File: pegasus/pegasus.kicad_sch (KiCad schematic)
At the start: 14 parts, among them IC4 L70B-M39, IC5 L7805ACV, J1 Conn_01x02_Female, J2 Conn_01x02_Female, U1 Teensy4.1

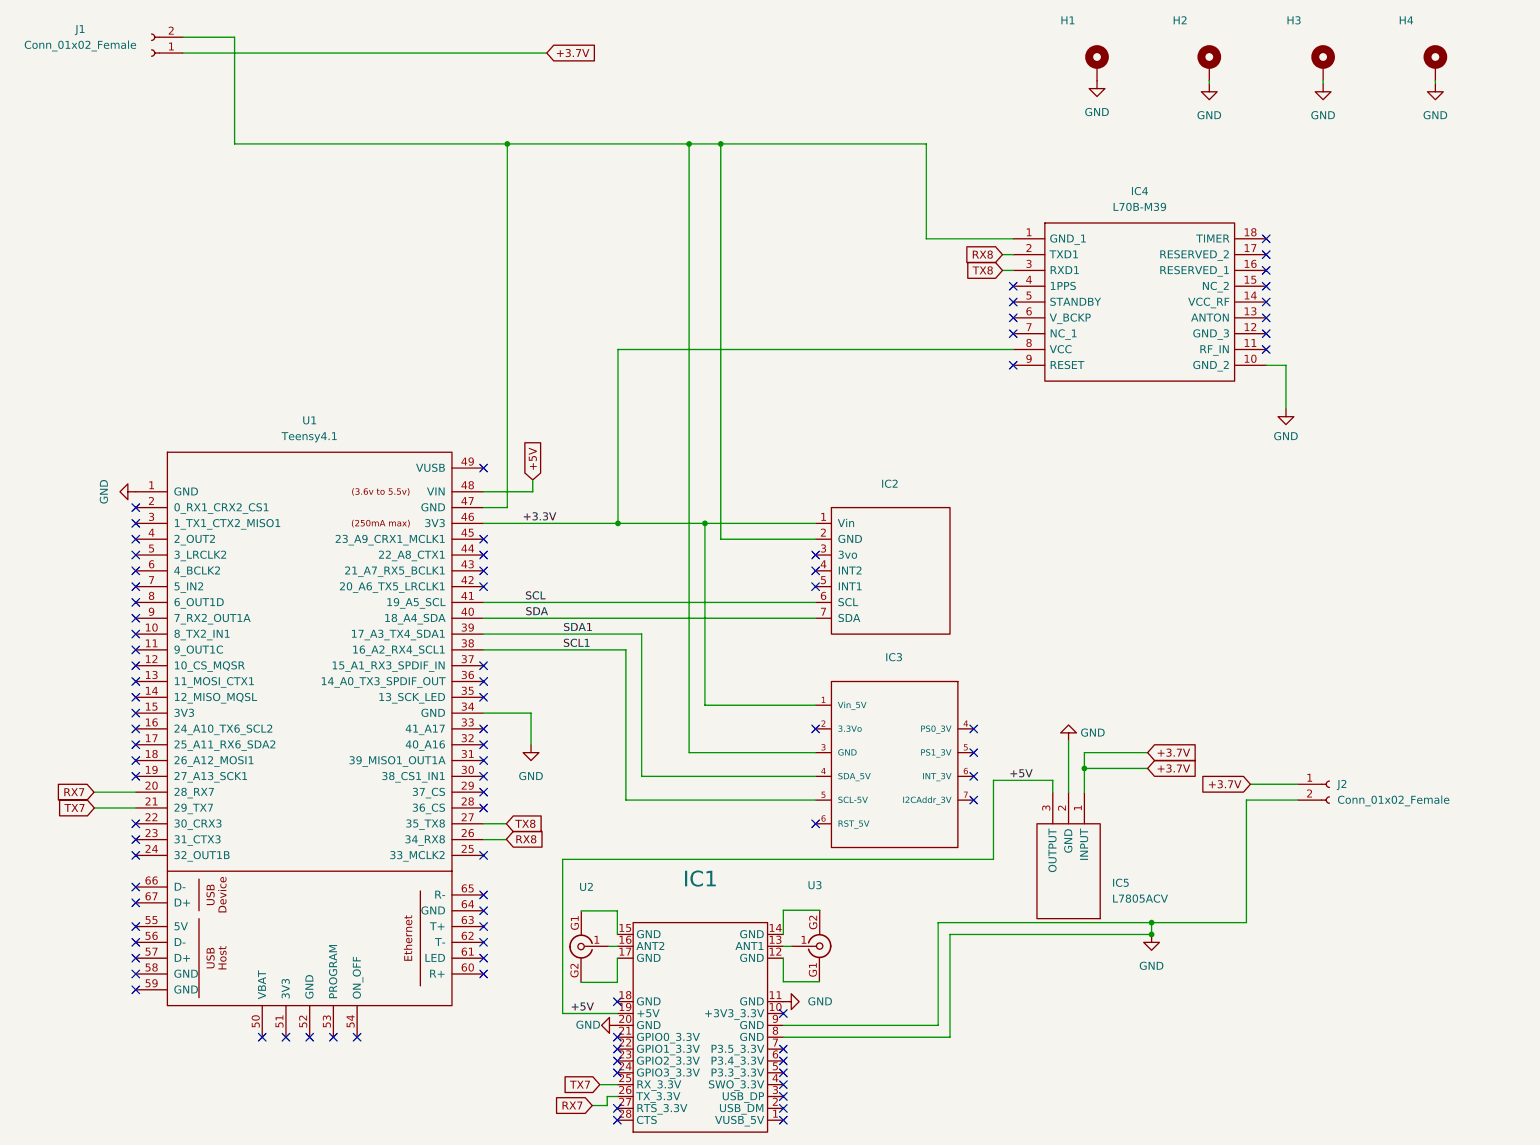
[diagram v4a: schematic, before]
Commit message: fixed BNO055 pin numbering, cleaned up schematic
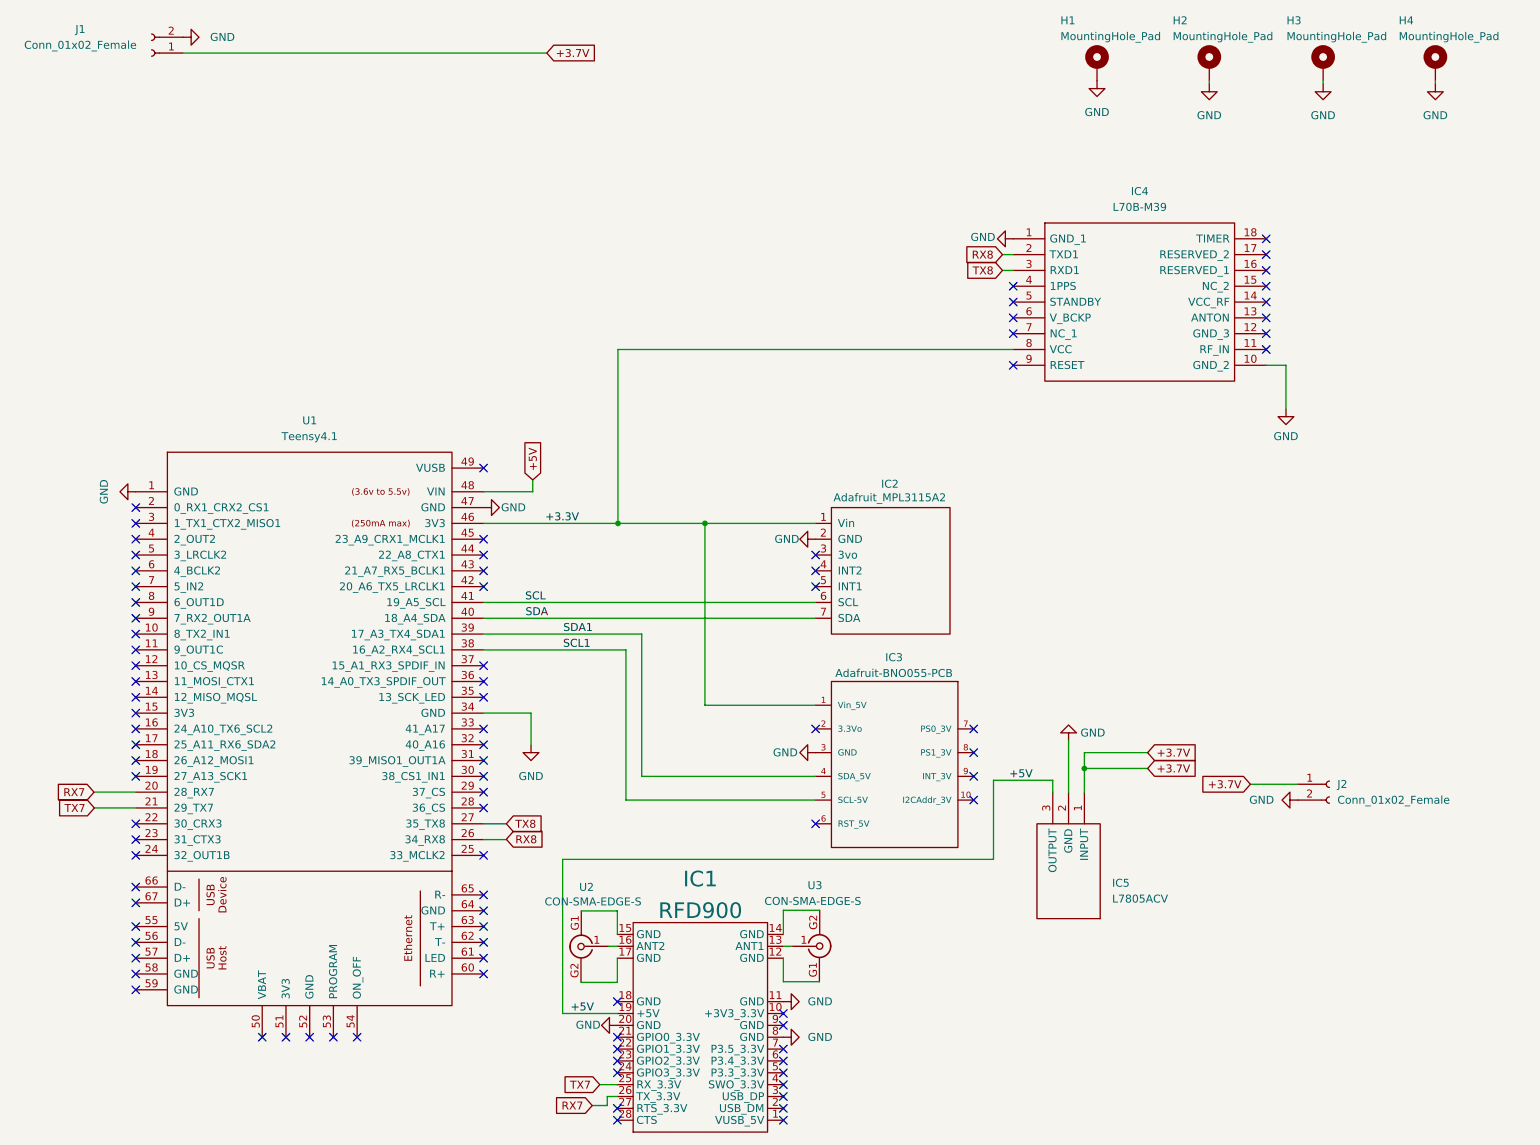
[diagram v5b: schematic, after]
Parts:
- H1, H2, H3, H4: value (none) -> MountingHole_Pad; footprint (none) -> MountingHole:MountingHole_2.2mm_M2_Pad
- IC1: value (none) -> RFD900
- IC2: value (none) -> Adafruit_MPL3115A2
- IC3: value (none) -> Adafruit-BNO055-PCB
- U2, U3: value (none) -> CON-SMA-EDGE-S; footprint (none) -> SMA-Connectors:RFSOLUTIONS_CON-SMA-EDGE-S
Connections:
- net GND: now also IC2.2 (GND), IC3.3 (GND), IC4.1 (GND_1), J1.2 (Pin_2), U1.47 (GND); no longer IC1.9 (GND)
- no-connect marks 91 -> 92
